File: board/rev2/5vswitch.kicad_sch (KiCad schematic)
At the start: 15 parts, among them Q1 WSD40120DN56G, U3 TPS259472A, U4 LM5050-1

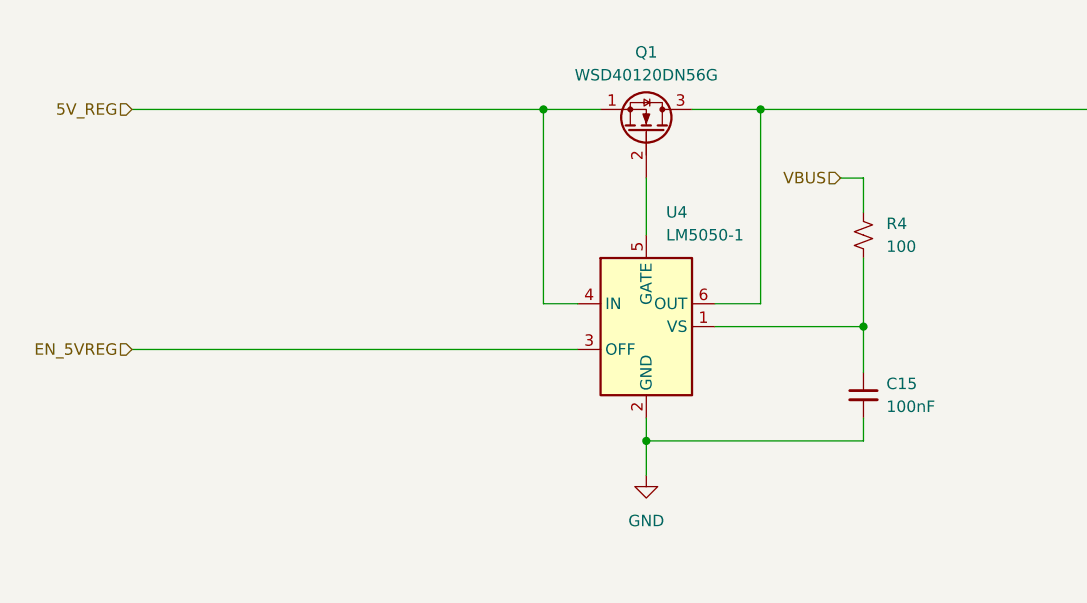
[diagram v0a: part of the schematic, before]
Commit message: Board REVB - fix 5V mux and add discharge path
also, fix a few routing issues
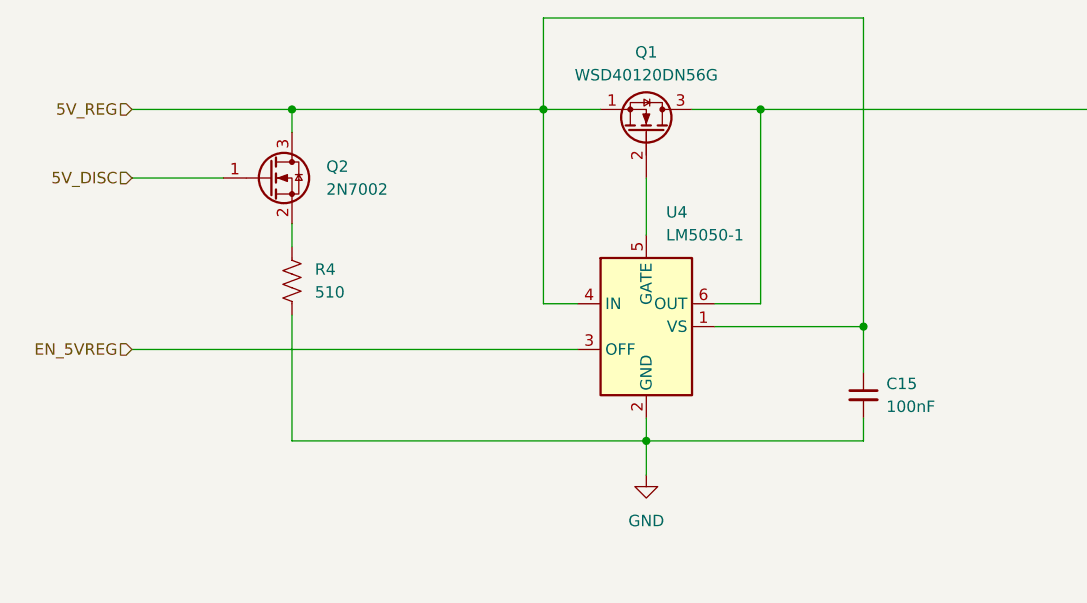
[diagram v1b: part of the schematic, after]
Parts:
- removed R4: 100, Resistor_SMD:R_1206_3216Metric, symbol Device:R_Small_US
- added Q2: 2N7002, Package_TO_SOT_SMD:SOT-23, symbol Transistor_FET:Q_NMOS_GSD
- added R4: 510, Resistor_SMD:R_0603_1608Metric, symbol Device:R_US
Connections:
- net 5V_REG: now also C15.1, U4.1 (VS), Q2.3 (D)
- net GND: now also R4.2
- new net: Q2.2 (S), R4.1
- new net 5V_DISC: Q2.1 (G)
